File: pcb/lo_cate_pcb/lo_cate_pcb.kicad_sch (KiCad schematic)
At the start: 9 parts, among them SW1 PTS 647 SN50 SMTR2 LFS, SW2 PTS 647 SN50 SMTR2 LFS, SW3 PTS 647 SN50 SMTR2 LFS, SW4 PTS 647 SN50 SMTR2 LFS, U1 STM32F401RETx, U2 BMI323, U3 150141M173100, U4 150141M173100, U5 150141M173100

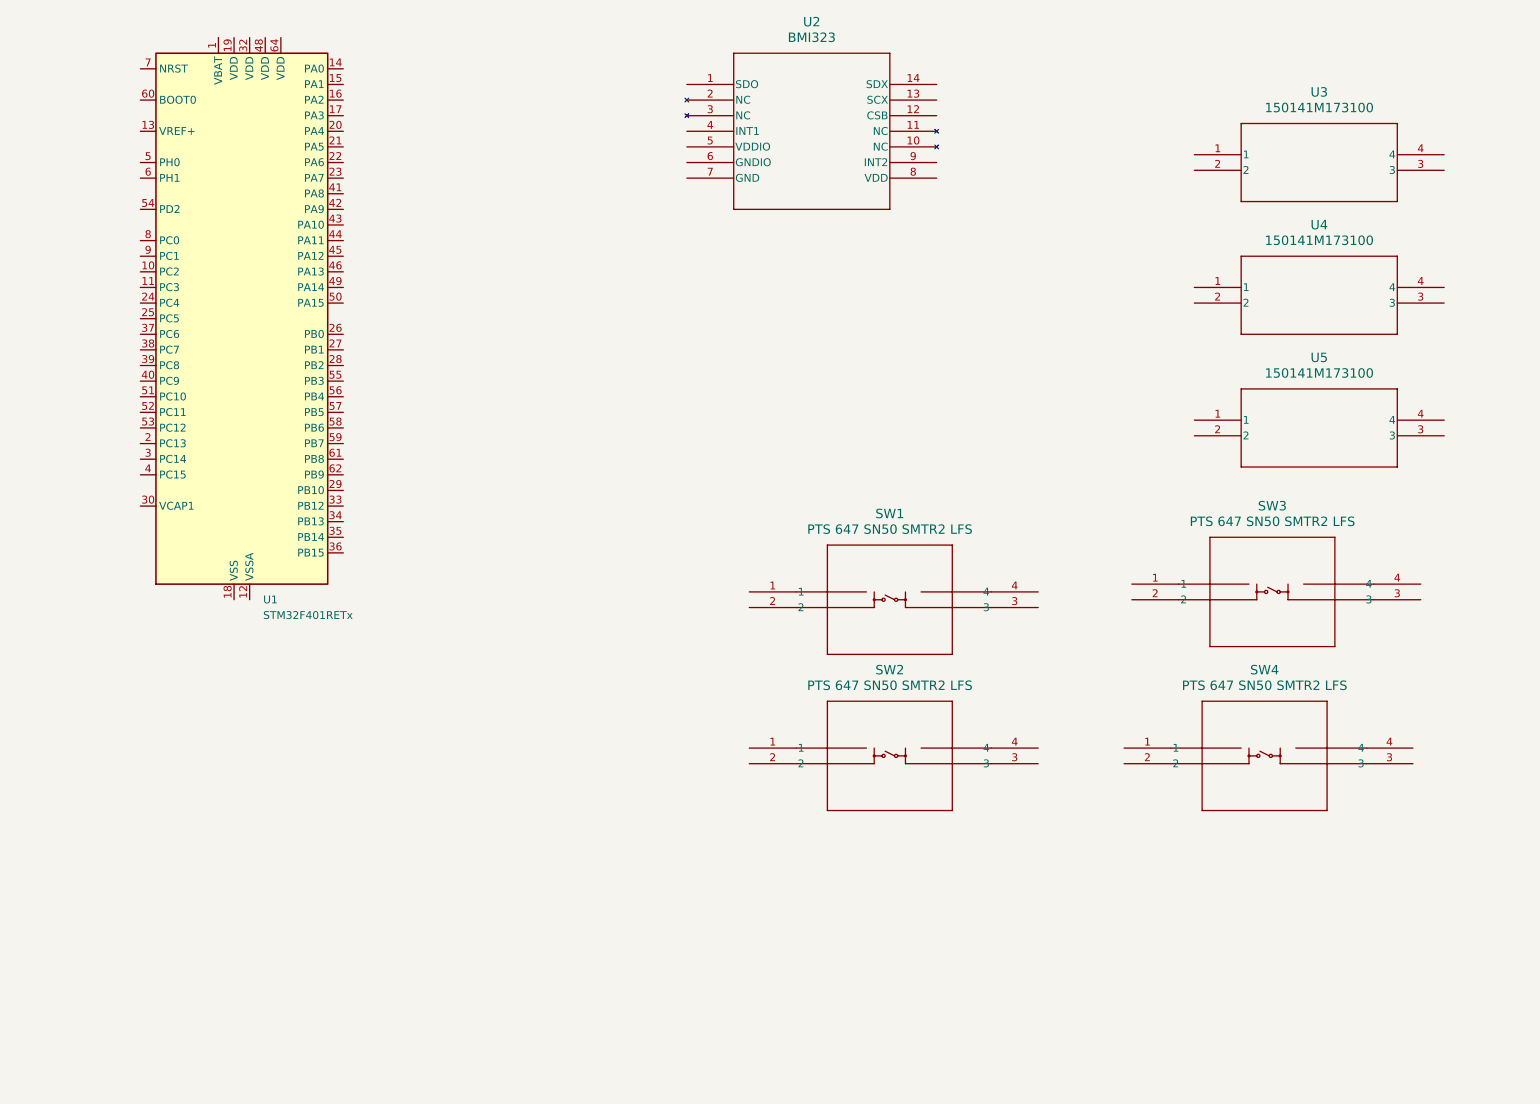
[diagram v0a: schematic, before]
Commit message: Finished basic PCB connections, now need to do the power electronics and antenna
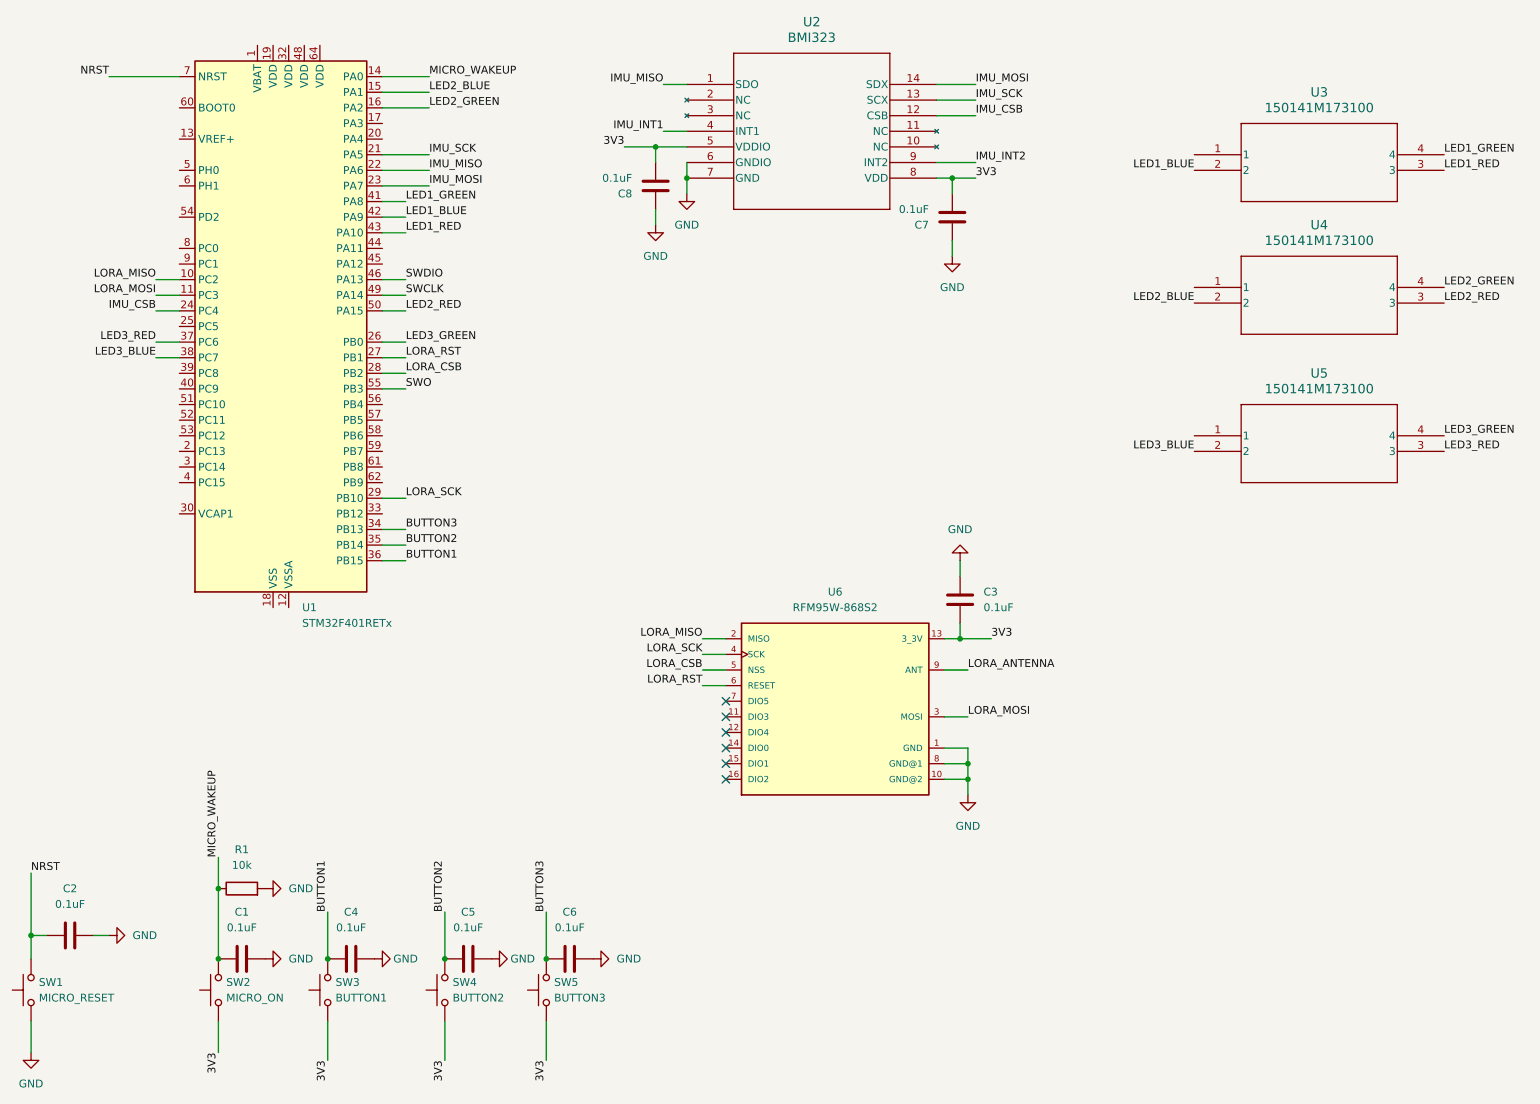
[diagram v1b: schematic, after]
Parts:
- removed SW1, SW2, SW3, SW4: PTS 647 SN50 SMTR2 LFS, PTS 647 SN50 SMTR2 LFS, symbol 2024-06-21_22-59-25:PTS_647_SN50_SMTR2_LFS
- added C1, C2, C3, C4, C5, C6, C7, C8: 0.1uF, symbol Device:C
- added R1: 10k, symbol Device:R
- added SW1: MICRO_RESET, symbol Switch:SW_Push
- added SW2: MICRO_ON, symbol Switch:SW_Push
- added SW3: BUTTON1, symbol Switch:SW_Push
- added SW4: BUTTON2, symbol Switch:SW_Push
- added SW5: BUTTON3, symbol Switch:SW_Push
- added U6: RFM95W-868S2, RFM95W-868S2:XCVR_RFM95W-868S2, symbol RFM95W-868S2:RFM95W-868S2
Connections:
- net LED2_BLUE: now reaches U4.2
- net LED2_BLUE: now also U1.15 (PA1)
- net LED2_RED: now reaches U4.3
- net LED2_RED: now also U1.50 (PA15)
- net LED2_GREEN: now reaches U4.4
- net LED2_GREEN: now also U1.16 (PA2)
- net LORA_MISO: now reaches U1.10 (PC2)
- net LORA_MISO: now also U6.2 (MISO)
- net LORA_MOSI: now reaches U1.11 (PC3)
- net LORA_MOSI: now also U6.3 (MOSI)
- net MICRO_WAKEUP: now reaches U1.14 (PA0)
- net MICRO_WAKEUP: now also C1.2, R1.1, SW2.2
- net IMU_SCK: now reaches U1.21 (PA5)
- net IMU_SCK: now also U2.13 (SCX)
- net IMU_MISO: now reaches U1.22 (PA6)
- net IMU_MISO: now also U2.1 (SDO)
- net IMU_MOSI: now reaches U1.23 (PA7)
- net IMU_MOSI: now also U2.14 (SDX)
- net IMU_CSB: now reaches U1.24 (PC4)
- net IMU_CSB: now also U2.12 (CSB)
- net LED3_GREEN: now reaches U1.26 (PB0)
- net LED3_GREEN: now also U5.4
- net LORA_RST: now reaches U1.27 (PB1)
- net LORA_RST: now also U6.6 (RESET)
- net LORA_CSB: now reaches U1.28 (PB2)
- net LORA_CSB: now also U6.5 (NSS)
- net LORA_SCK: now reaches U1.29 (PB10)
- net LORA_SCK: now also U6.4 (SCK)
- net BUTTON3: now reaches U1.34 (PB13)
- net BUTTON3: now also C6.2, SW5.2
- net BUTTON2: now reaches U1.35 (PB14)
- net BUTTON2: now also C5.2, SW4.2
- net BUTTON1: now reaches U1.36 (PB15)
- net BUTTON1: now also C4.2, SW3.2
- net LED3_RED: now reaches U1.37 (PC6)
- net LED3_RED: now also U5.3
- net LED3_BLUE: now reaches U1.38 (PC7)
- net LED3_BLUE: now also U5.2
- net LED1_GREEN: now reaches U1.41 (PA8)
- net LED1_GREEN: now also U3.4
- net LED1_BLUE: now reaches U1.42 (PA9)
- net LED1_BLUE: now also U3.2
- net LED1_RED: now reaches U1.43 (PA10)
- net LED1_RED: now also U3.3
- net SWDIO: now reaches U1.46 (PA13)
- net SWCLK: now reaches U1.49 (PA14)
- net SWO: now reaches U1.55 (PB3)
- net NRST: now reaches U1.7 (NRST)
- net NRST: now also C2.2, SW1.2
- net IMU_INT1: now reaches U2.4 (INT1)
- net 3V3: now reaches U2.5 (VDDIO)
- net 3V3: now also U2.8 (VDD), C3.2, C7.2, C8.2, SW2.1, SW3.1, SW4.1, SW5.1, U6.13 (3_3V)
- net GND: now reaches U2.6 (GNDIO)
- net GND: now also U2.7 (GND), C1.1, C2.1, C3.1, C4.1, C5.1, C6.1, C7.1, C8.1, R1.2, SW1.1, U6.1 (GND), U6.10 (GND@2), U6.8 (GND@1)
- net IMU_INT2: now reaches U2.9 (INT2)
- new net LORA_ANTENNA: U6.9 (ANT)
- no-connect marks 0 -> 6
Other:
- moved on the sheet: U1
